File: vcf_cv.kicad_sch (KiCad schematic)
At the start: 24 parts

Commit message: VCF schem combed
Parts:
- C701, C702: renamed from C?; footprint (none) -> Capacitor_SMD:C_0603_1608Metric_Pad1.08x0.95mm_HandSolder
- D703, D704: renamed from D?; footprint (none) -> Diode_SMD:D_SOD-323_HandSoldering
- R701, R702, R703, R704, R705, R706, R707, R708: renamed from R?; footprint (none) -> Resistor_SMD:R_0603_1608Metric_Pad0.98x0.95mm_HandSolder
- U701: renamed from U?; footprint (none) -> Package_SO:SOIC-14_3.9x8.7mm_P1.27mm
- U702: renamed from U?; footprint (none) -> Package_SO:SOIC-8_3.9x4.9mm_P1.27mm
- gave numbers to parts that had none: 4
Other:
- note added: "Limit min voltage to +4.5V"

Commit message: WIP VCF Layout
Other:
- note added: "Limits min voltage to +4.5V"
- note removed: "Limit min voltage to +4.5V"
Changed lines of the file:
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@@
     (stroke (width 0) (type default) (color 0 0 0 0))
   )
-  (text "Limit min voltage to +4.5V" (at 63.5 45.72 0)
+  (text "Limits min voltage to +4.5V" (at 63.5 45.72 0)
     (effects (font (size 1.27 1.27)) (justify left bottom))
   )

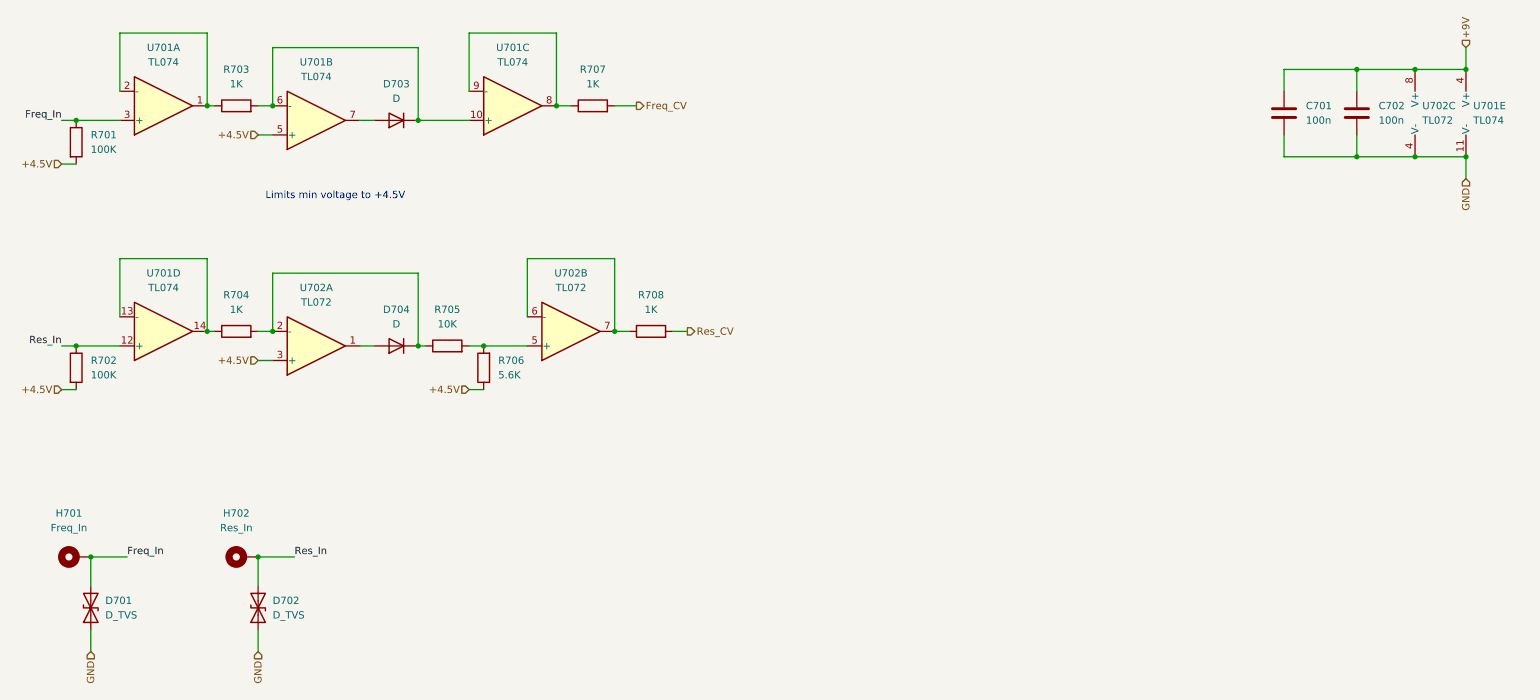
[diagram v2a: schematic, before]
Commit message: Switch VCF cv processing opamps
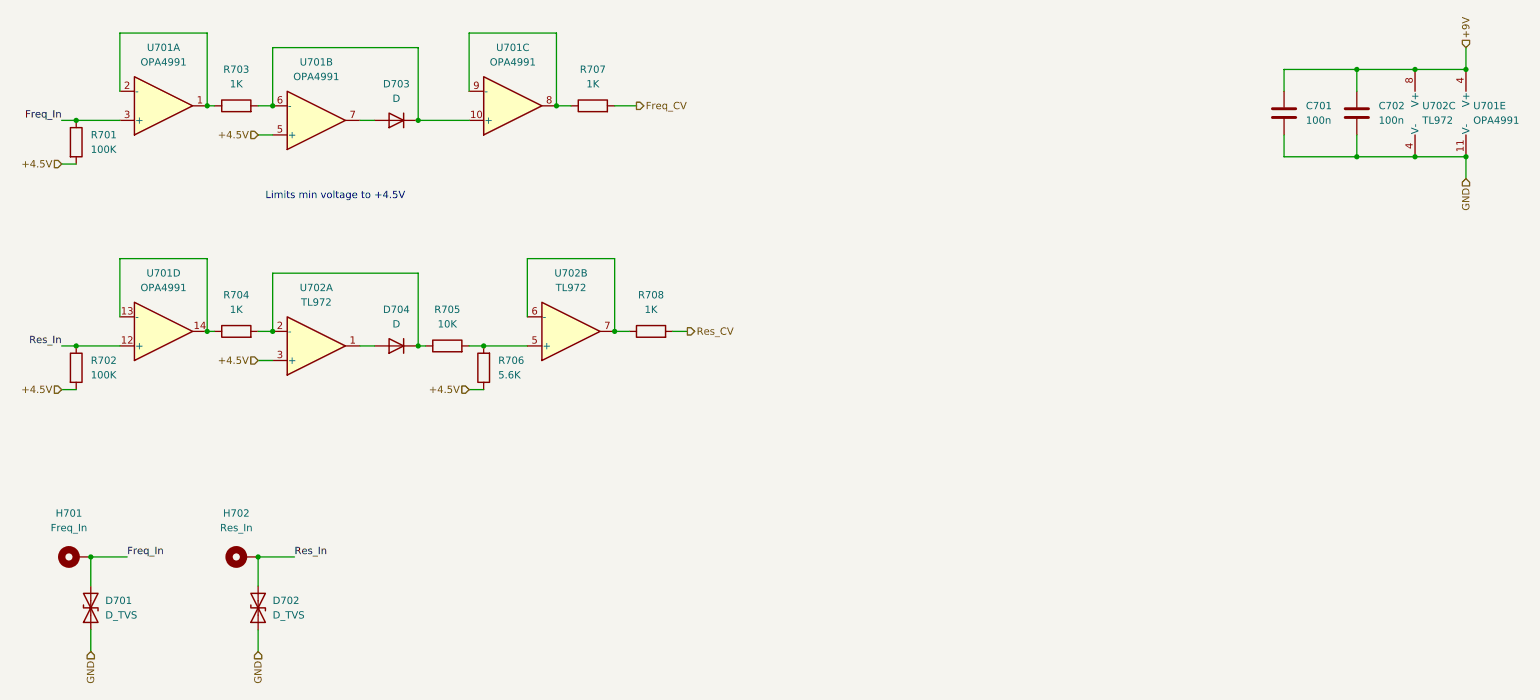
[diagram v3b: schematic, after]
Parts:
- U701: value TL074 -> OPA4991
- U702: value TL072 -> TL972
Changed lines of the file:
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@@
       (effects (font (size 1.27 1.27)) (justify left))
     )
-    (property "Value" "TL072" (id 1) (at 265.43 31.7499 0)
+    (property "Value" "TL972" (id 1) (at 265.43 31.7499 0)
       (effects (font (size 1.27 1.27)) (justify left))
     )
@@
     (in_bom yes) (on_board yes) (fields_autoplaced)
     (property "Reference" "U701" (id 0) (at 45.72 19.05 0))
-    (property "Value" "TL074" (id 1) (at 45.72 21.59 0))
+    (property "Value" "OPA4991" (id 1) (at 45.72 21.59 0))
     (property "Footprint" "Package_SO:SOIC-14_3.9x8.7mm_P1.27mm" (id 2) (at 44.45 31.75 0)
       (effects (font (size 1.27 1.27)) hide)
@@
     (in_bom yes) (on_board yes) (fields_autoplaced)
     (property "Reference" "U701" (id 0) (at 45.72 58.42 0))
-    (property "Value" "TL074" (id 1) (at 45.72 60.96 0))
+    (property "Value" "OPA4991" (id 1) (at 45.72 60.96 0))
     (property "Footprint" "Package_SO:SOIC-14_3.9x8.7mm_P1.27mm" (id 2) (at 44.45 71.12 0)
       (effects (font (size 1.27 1.27)) hide)
@@
     (in_bom yes) (on_board yes) (fields_autoplaced)
     (property "Reference" "U701" (id 0) (at 106.68 19.05 0))
-    (property "Value" "TL074" (id 1) (at 106.68 21.59 0))
+    (property "Value" "OPA4991" (id 1) (at 106.68 21.59 0))
     (property "Footprint" "Package_SO:SOIC-14_3.9x8.7mm_P1.27mm" (id 2) (at 105.41 31.75 0)
       (effects (font (size 1.27 1.27)) hide)
@@
       (effects (font (size 1.27 1.27)) (justify left))
     )
-    (property "Value" "TL074" (id 1) (at 274.32 31.7499 0)
+    (property "Value" "OPA4991" (id 1) (at 274.32 31.7499 0)
       (effects (font (size 1.27 1.27)) (justify left))
     )
@@
     (in_bom yes) (on_board yes) (fields_autoplaced)
     (property "Reference" "U702" (id 0) (at 72.39 60.96 0))
-    (property "Value" "TL072" (id 1) (at 72.39 63.5 0))
+    (property "Value" "TL972" (id 1) (at 72.39 63.5 0))
     (property "Footprint" "Package_SO:SOIC-8_3.9x4.9mm_P1.27mm" (id 2) (at 72.39 71.12 0)
       (effects (font (size 1.27 1.27)) hide)
@@
     (in_bom yes) (on_board yes) (fields_autoplaced)
     (property "Reference" "U701" (id 0) (at 72.39 21.59 0))
-    (property "Value" "TL074" (id 1) (at 72.39 24.13 0))
+    (property "Value" "OPA4991" (id 1) (at 72.39 24.13 0))
     (property "Footprint" "Package_SO:SOIC-14_3.9x8.7mm_P1.27mm" (id 2) (at 71.12 34.29 0)
       (effects (font (size 1.27 1.27)) hide)
@@
     (in_bom yes) (on_board yes) (fields_autoplaced)
     (property "Reference" "U702" (id 0) (at 116.84 58.42 0))
-    (property "Value" "TL072" (id 1) (at 116.84 60.96 0))
+    (property "Value" "TL972" (id 1) (at 116.84 60.96 0))
     (property "Footprint" "Package_SO:SOIC-8_3.9x4.9mm_P1.27mm" (id 2) (at 116.84 68.58 0)
       (effects (font (size 1.27 1.27)) hide)

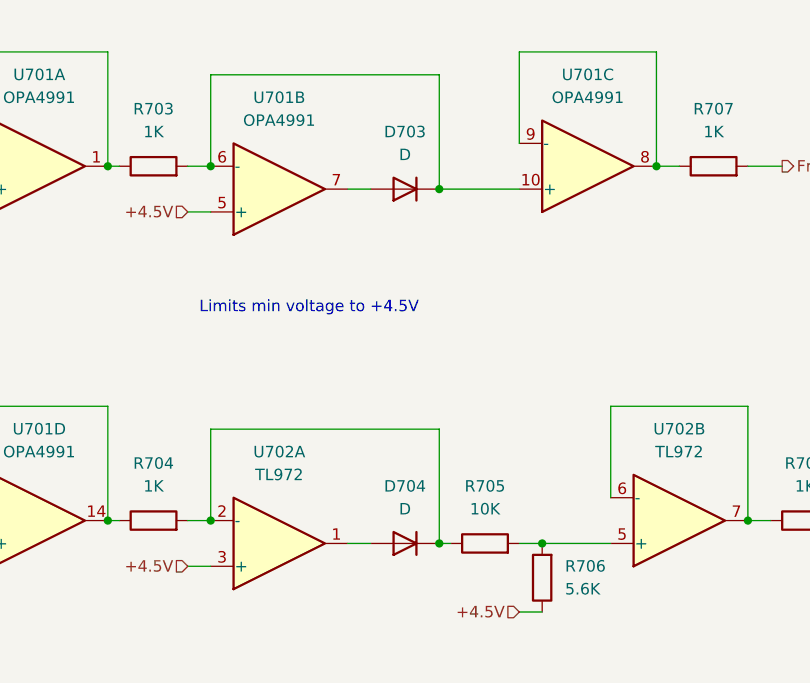
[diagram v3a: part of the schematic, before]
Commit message: Add JLC parts numbers
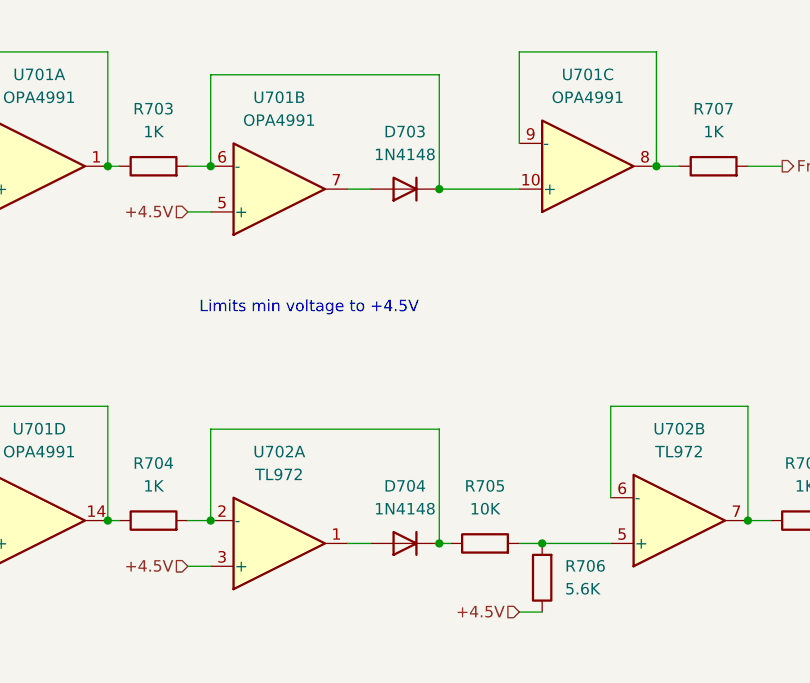
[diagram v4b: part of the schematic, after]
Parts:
- C701, C702: LCSC (none) -> C497032; Role (none) -> ic-bypass
- D701, D702: LCSC (none) -> C20936
- D703, D704: value D -> 1N4148; LCSC (none) -> C2128
- R701, R702: LCSC (none) -> C14675
- R703, R704, R707, R708: LCSC (none) -> C2907002
- R705: LCSC (none) -> C98220
- R706: LCSC (none) -> C365194
- U701: LCSC (none) -> C2860973
- U702: LCSC (none) -> C46127
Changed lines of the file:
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@@
+      (effects (font (size 1.27 1.27)) hide)
+    )
+    (property "LCSC" "C2907002" (id 4) (at 58.42 29.21 0)
       (effects (font (size 1.27 1.27)) hide)
     )
@@
       (effects (font (size 1.27 1.27)) hide)
     )
-    (property "Datasheet" "http://www.ti.com/lit/ds/symlink/tl071.pdf" (id 3) (at 266.7 30.48 0)
+    (property "Datasheet" "http://ww1.microchip.com/downloads/en/DeviceDoc/21733j.pdf" (id 3) (at 266.7 30.48 0)
+      (effects (font (size 1.27 1.27)) hide)
+    )
+    (property "LCSC" "C46127" (id 4) (at 266.7 30.48 0)
       (effects (font (size 1.27 1.27)) hide)
     )
@@
       (effects (font (size 1.27 1.27)) hide)
     )
+    (property "LCSC" "C14675" (id 4) (at 30.48 35.56 0)
+      (effects (font (size 1.27 1.27)) hide)
+    )
     (pin "1")
     (pin "2")
@@
     (in_bom yes) (on_board yes) (fields_autoplaced)
     (property "Reference" "D703" (id 0) (at 86.36 25.4 0))
-    (property "Value" "D" (id 1) (at 86.36 27.94 0))
+    (property "Value" "1N4148" (id 1) (at 86.36 27.94 0))
     (property "Footprint" "Diode_SMD:D_SOD-323_HandSoldering" (id 2) (at 86.36 31.75 0)
       (effects (font (size 1.27 1.27)) hide)
     )
     (property "Datasheet" "~" (id 3) (at 86.36 31.75 0)
+      (effects (font (size 1.27 1.27)) hide)
+    )
+    (property "LCSC" "C2128" (id 4) (at 86.36 31.75 0)
       (effects (font (size 1.27 1.27)) hide)
     )
@@
       (effects (font (size 1.27 1.27)) hide)
     )
+    (property "LCSC" "C2907002" (id 4) (at 130.81 68.58 0)
+      (effects (font (size 1.27 1.27)) hide)
+    )
     (pin "1")
     (pin "2")
@@
       (effects (font (size 1.27 1.27)) hide)
     )
+    (property "LCSC" "C2907002" (id 4) (at 120.65 29.21 0)
+      (effects (font (size 1.27 1.27)) hide)
+    )
     (pin "1")
     (pin "2")
@@
     )
     (property "Datasheet" "~" (id 3) (at 33.02 116.84 0)
+      (effects (font (size 1.27 1.27)) hide)
+    )
+    (property "LCSC" "C20936" (id 4) (at 33.02 116.84 0)
       (effects (font (size 1.27 1.27)) hide)
     )
@@
       (effects (font (size 1.27 1.27)) hide)
     )
-    (property "Datasheet" "http://www.ti.com/lit/ds/symlink/tl071.pdf" (id 3) (at 46.99 34.29 0)
+    (property "Datasheet" "http://ww1.microchip.com/downloads/en/DeviceDoc/21733j.pdf" (id 3) (at 46.99 34.29 0)
+      (effects (font (size 1.27 1.27)) hide)
+    )
+    (property "LCSC" "C2860973" (id 4) (at 45.72 29.21 0)
       (effects (font (size 1.27 1.27)) hide)
     )
@@
       (effects (font (size 1.27 1.27)) hide)
     )
-    (property "Datasheet" "http://www.ti.com/lit/ds/symlink/tl071.pdf" (id 3) (at 46.99 73.66 0)
+    (property "Datasheet" "http://ww1.microchip.com/downloads/en/DeviceDoc/21733j.pdf" (id 3) (at 46.99 73.66 0)
+      (effects (font (size 1.27 1.27)) hide)
+    )
+    (property "LCSC" "C2860973" (id 4) (at 45.72 68.58 0)
       (effects (font (size 1.27 1.27)) hide)
     )
@@
       (effects (font (size 1.27 1.27)) hide)
     )
-    (property "Datasheet" "http://www.ti.com/lit/ds/symlink/tl071.pdf" (id 3) (at 107.95 34.29 0)
+    (property "Datasheet" "http://ww1.microchip.com/downloads/en/DeviceDoc/21733j.pdf" (id 3) (at 107.95 34.29 0)
+      (effects (font (size 1.27 1.27)) hide)
+    )
+    (property "LCSC" "C2860973" (id 4) (at 106.68 29.21 0)
       (effects (font (size 1.27 1.27)) hide)
     )
@@
     (in_bom yes) (on_board yes) (fields_autoplaced)
     (property "Reference" "D704" (id 0) (at 86.36 64.77 0))
-    (property "Value" "D" (id 1) (at 86.36 67.31 0))
+    (property "Value" "1N4148" (id 1) (at 86.36 67.31 0))
     (property "Footprint" "Diode_SMD:D_SOD-323_HandSoldering" (id 2) (at 86.36 71.12 0)
       (effects (font (size 1.27 1.27)) hide)
@@
       (effects (font (size 1.27 1.27)) hide)
     )
+    (property "LCSC" "C2128" (id 4) (at 86.36 71.12 0)
+      (effects (font (size 1.27 1.27)) hide)
+    )
     (pin "1")
     (pin "2")
@@
       (effects (font (size 1.27 1.27)) hide)
     )
-    (property "Datasheet" "http://www.ti.com/lit/ds/symlink/tl071.pdf" (id 3) (at 276.86 25.4 0)
+    (property "Datasheet" "http://ww1.microchip.com/downloads/en/DeviceDoc/21733j.pdf" (id 3) (at 276.86 25.4 0)
+      (effects (font (size 1.27 1.27)) hide)
+    )
+    (property "LCSC" "C2860973" (id 4) (at 275.59 30.48 0)
       (effects (font (size 1.27 1.27)) hide)
     )
@@
       (effects (font (size 1.27 1.27)) hide)
     )
+    (property "LCSC" "C98220" (id 4) (at 95.25 71.12 0)
+      (effects (font (size 1.27 1.27)) hide)
+    )
     (pin "1")
     (pin "2")
@@
       (effects (font (size 1.27 1.27)) hide)
     )
+    (property "LCSC" "C14675" (id 4) (at 30.48 74.93 0)
+      (effects (font (size 1.27 1.27)) hide)
+    )
     (pin "1")
     (pin "2")
@@
     )
     (property "Datasheet" "~" (id 3) (at 62.23 116.84 0)
+      (effects (font (size 1.27 1.27)) hide)
+    )
+    (property "LCSC" "C20936" (id 4) (at 62.23 116.84 0)
       (effects (font (size 1.27 1.27)) hide)
     )
@@
       (effects (font (size 1.27 1.27)) hide)
     )
+    (property "LCSC" "C365194" (id 4) (at 101.6 74.93 0)
+      (effects (font (size 1.27 1.27)) hide)
+    )
     (pin "1")
     (pin "2")
@@
       (effects (font (size 1.27 1.27)) hide)
     )
-    (property "Datasheet" "http://www.ti.com/lit/ds/symlink/tl071.pdf" (id 3) (at 72.39 71.12 0)
+    (property "Datasheet" "http://ww1.microchip.com/downloads/en/DeviceDoc/21733j.pdf" (id 3) (at 72.39 71.12 0)
+      (effects (font (size 1.27 1.27)) hide)
+    )
+    (property "LCSC" "C46127" (id 4) (at 72.39 71.12 0)
       (effects (font (size 1.27 1.27)) hide)
     )
@@
     )
     (property "Datasheet" "~" (id 3) (at 241.3 30.48 0)
+      (effects (font (size 1.27 1.27)) hide)
+    )
+    (property "LCSC" "C497032" (id 4) (at 241.3 30.48 0)
+      (effects (font (size 1.27 1.27)) hide)
+    )
+    (property "Role" "ic-bypass" (id 5) (at 241.3 30.48 0)
       (effects (font (size 1.27 1.27)) hide)
     )
@@
       (effects (font (size 1.27 1.27)) hide)
     )
-    (property "Datasheet" "http://www.ti.com/lit/ds/symlink/tl071.pdf" (id 3) (at 73.66 36.83 0)
+    (property "Datasheet" "http://ww1.microchip.com/downloads/en/DeviceDoc/21733j.pdf" (id 3) (at 73.66 36.83 0)
+      (effects (font (size 1.27 1.27)) hide)
+    )
+    (property "LCSC" "C2860973" (id 4) (at 72.39 31.75 0)
       (effects (font (size 1.27 1.27)) hide)
     )
@@
       (effects (font (size 1.27 1.27)) hide)
     )
+    (property "LCSC" "C497032" (id 4) (at 254 30.48 0)
+      (effects (font (size 1.27 1.27)) hide)
+    )
+    (property "Role" "ic-bypass" (id 5) (at 254 30.48 0)
+      (effects (font (size 1.27 1.27)) hide)
+    )
     (pin "1")
     (pin "2")
@@
       (effects (font (size 1.27 1.27)) hide)
     )
-    (property "Datasheet" "http://www.ti.com/lit/ds/symlink/tl071.pdf" (id 3) (at 116.84 68.58 0)
+    (property "Datasheet" "http://ww1.microchip.com/downloads/en/DeviceDoc/21733j.pdf" (id 3) (at 116.84 68.58 0)
+      (effects (font (size 1.27 1.27)) hide)
+    )
+    (property "LCSC" "C46127" (id 4) (at 116.84 68.58 0)
       (effects (font (size 1.27 1.27)) hide)
     )
@@
       (effects (font (size 1.27 1.27)) hide)
     )
+    (property "LCSC" "C2907002" (id 4) (at 58.42 68.58 0)
+      (effects (font (size 1.27 1.27)) hide)
+    )
